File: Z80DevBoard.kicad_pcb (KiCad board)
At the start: 2 copper layers, 143 parts, among them SW1 WAIT, SW2 RESET, SW3 Z80BOOT, SW4 RPBOOT

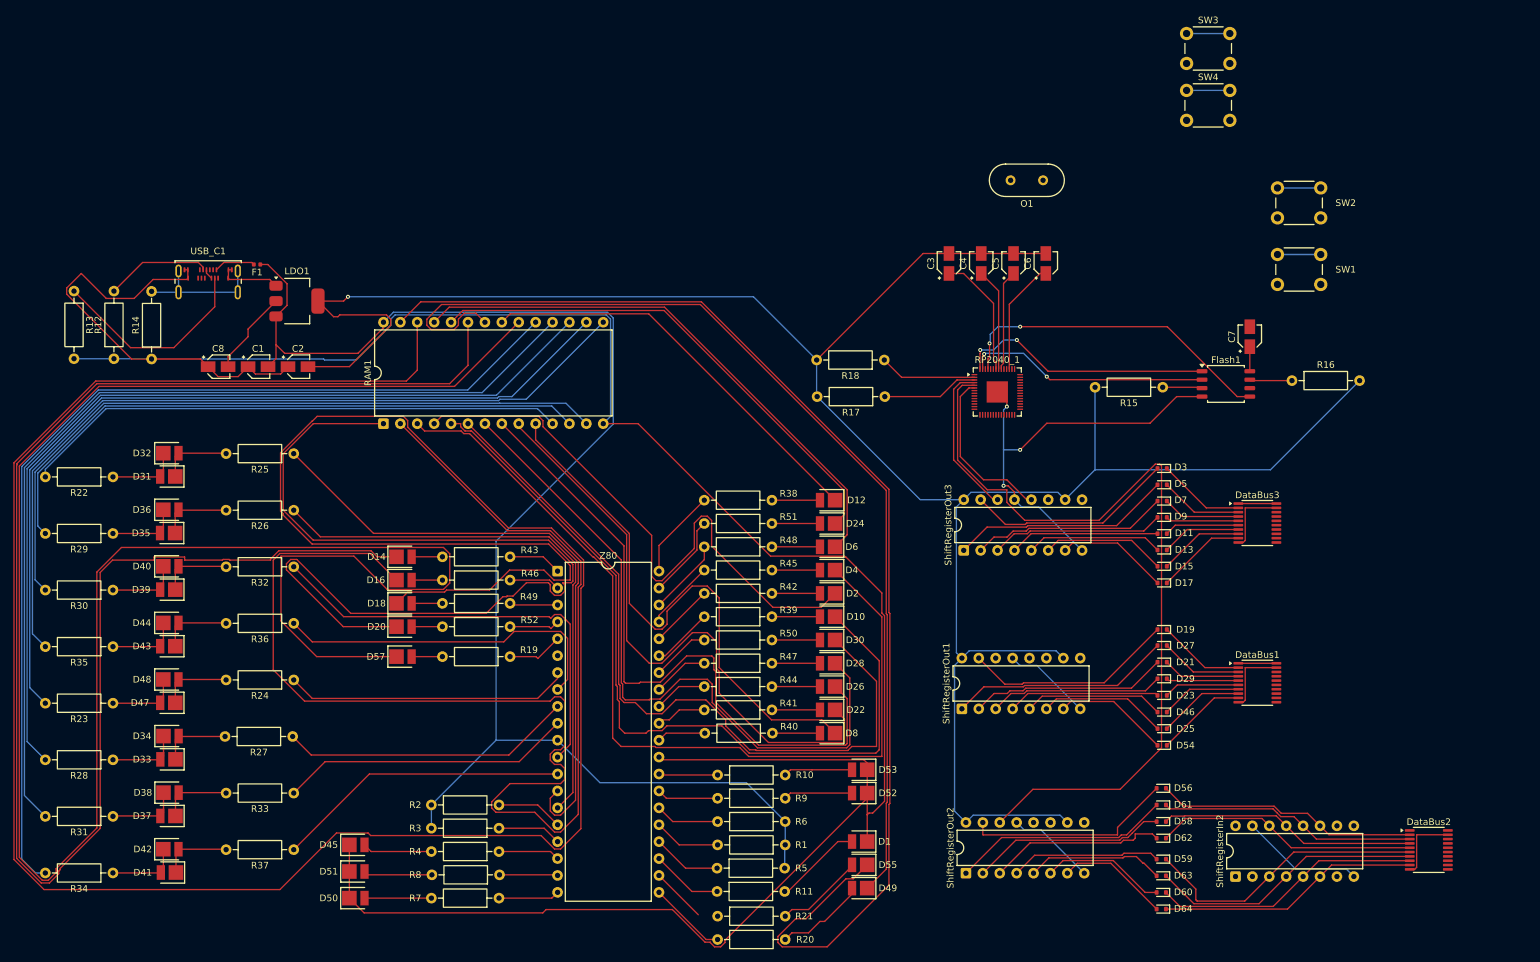
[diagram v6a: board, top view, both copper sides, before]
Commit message: Connected some pins of the RP2040. Connected the data bus to the RAM.
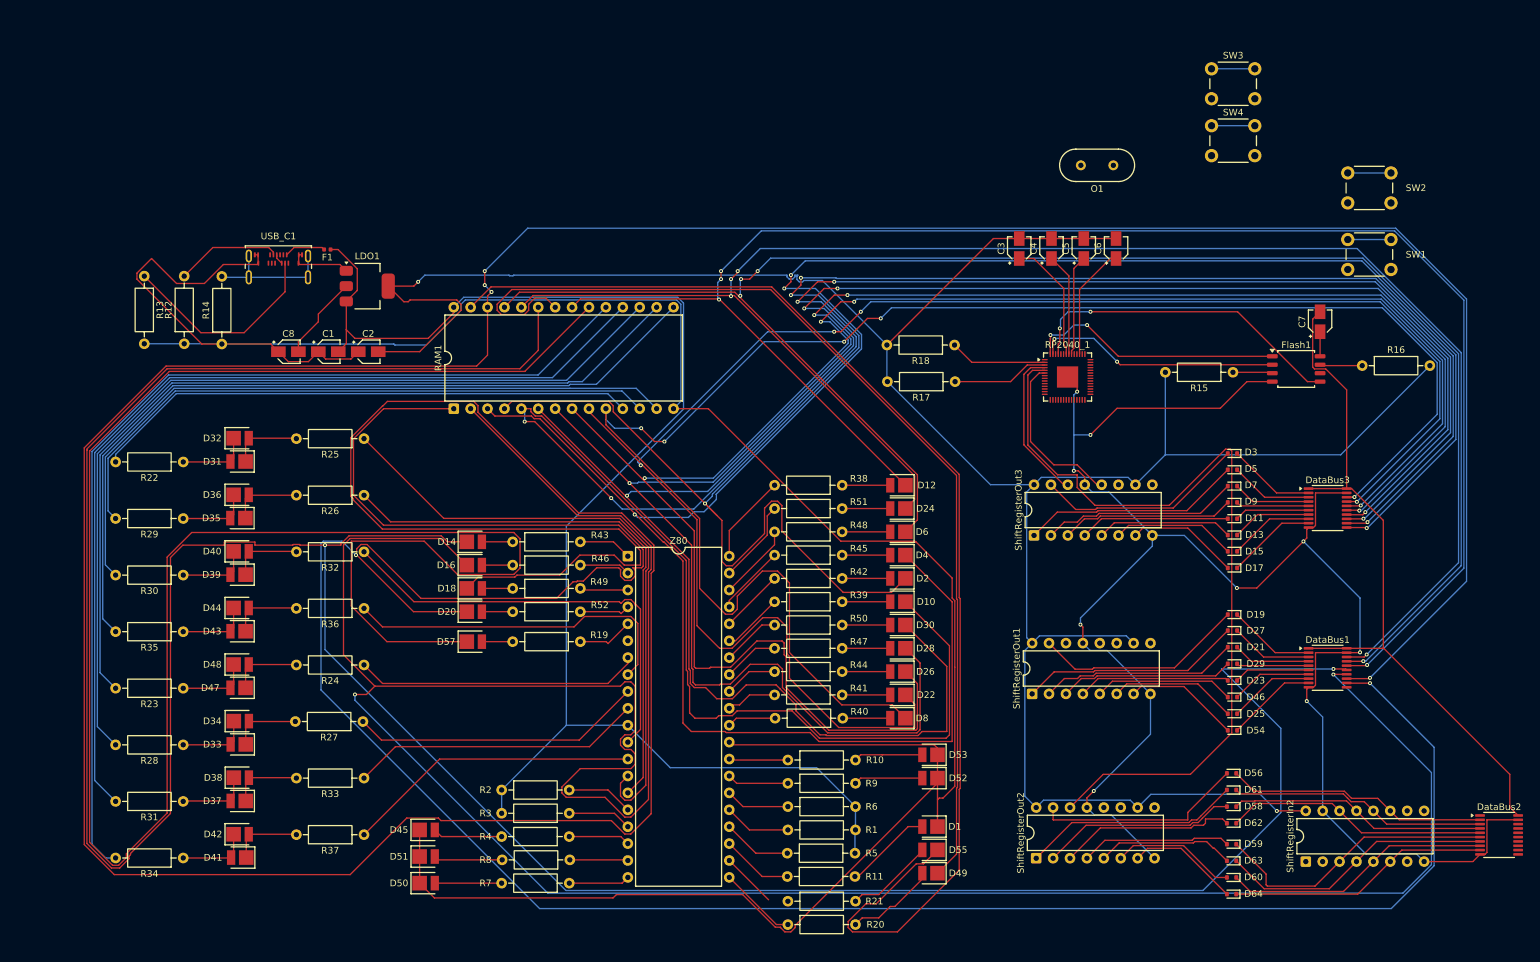
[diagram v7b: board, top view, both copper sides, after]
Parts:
- moved D56 10.8 mm to (212.8, 130.6)
- moved D58 10.8 mm to (212.8, 135.6)
- moved D61 10.8 mm to (212.8, 133.1)
- moved D62 10.8 mm to (212.8, 138.1)
- moved ShiftRegisterIn2 10.8 mm to (223.9, 143.9)
- moved ShiftRegisterOut2 10.8 mm to (183.4, 143.4)
- moved D10 10.8 mm to (162.9, 104.8)
- moved D12 10.8 mm to (162.9, 87.3)
- moved D2 10.8 mm to (162.9, 101.3)
- moved D22 10.8 mm to (162.9, 118.8)
- moved D24 10.8 mm to (162.9, 90.8)
- moved D26 10.8 mm to (162.9, 115.3)
- moved D28 10.8 mm to (162.9, 111.8)
- moved D30 10.8 mm to (162.9, 108.3)
- moved D4 10.8 mm to (162.9, 97.8)
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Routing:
- net RAM-A14: track 147.9 -> 394.6 mm, vias 0 -> 2
- net RAM-A13: track 410.6 -> 637.8 mm, vias 0 -> 4
- net RAM-A11: track 243.3 -> 466.6 mm, vias 0 -> 2
- net RAM-A12: track 200.8 -> 417.4 mm, vias 0 -> 2
- net RAM-A5: track 122.1 -> 338.4 mm, vias 0 -> 5
- net RAM-A7: track 135.7 -> 341.4 mm, vias 0 -> 4
- net RAM-A6: track 90.1 -> 279.8 mm, vias 0 -> 4
- net RAM-A4: track 113.6 -> 301.1 mm, vias 0 -> 4
- net RAM-A10: track 62.2 -> 249.1 mm, vias 0 -> 4
- net RAM-A3: track 104.5 -> 284.4 mm, vias 0 -> 4
- net RAM-A9: track 76.5 -> 252.5 mm, vias 0 -> 4
- net RAM-A2: track 100.4 -> 272.7 mm, vias 0 -> 4
- net RAM-A8: track 83.7 -> 255.5 mm, vias 0 -> 4
- net RAM-A0: track 84.5 -> 250.6 mm, vias 0 -> 5
- net RAM-A1: track 92.0 -> 254.9 mm, vias 0 -> 4
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
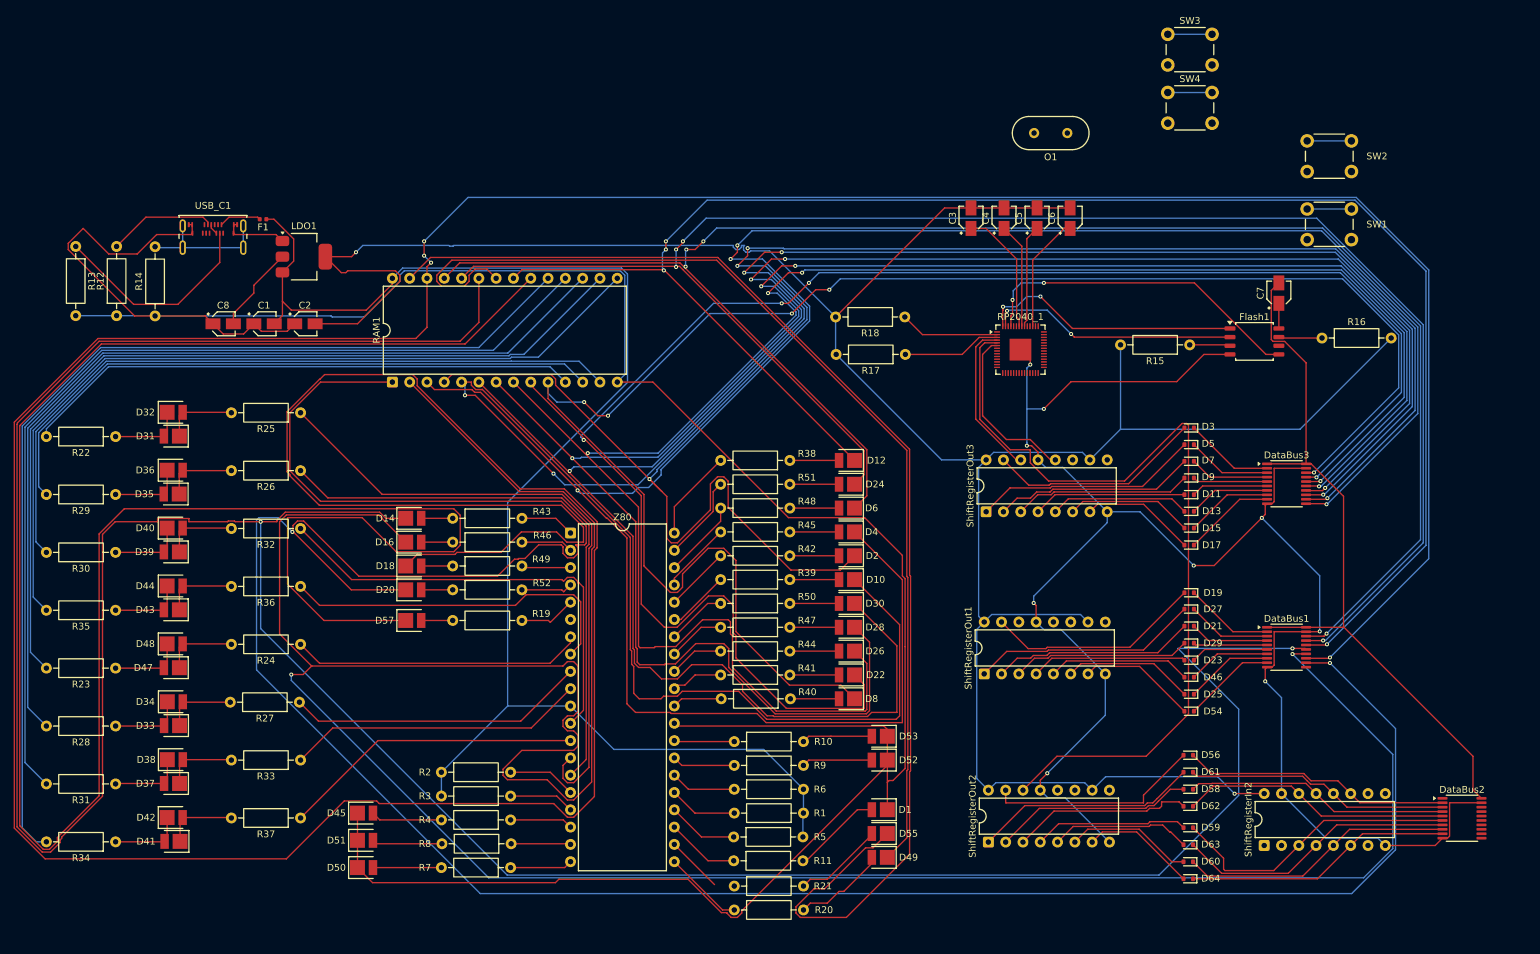
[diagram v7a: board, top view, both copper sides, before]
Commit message: Defined the boards. Positioned the last components. Do some connections. Semplified some old connections.
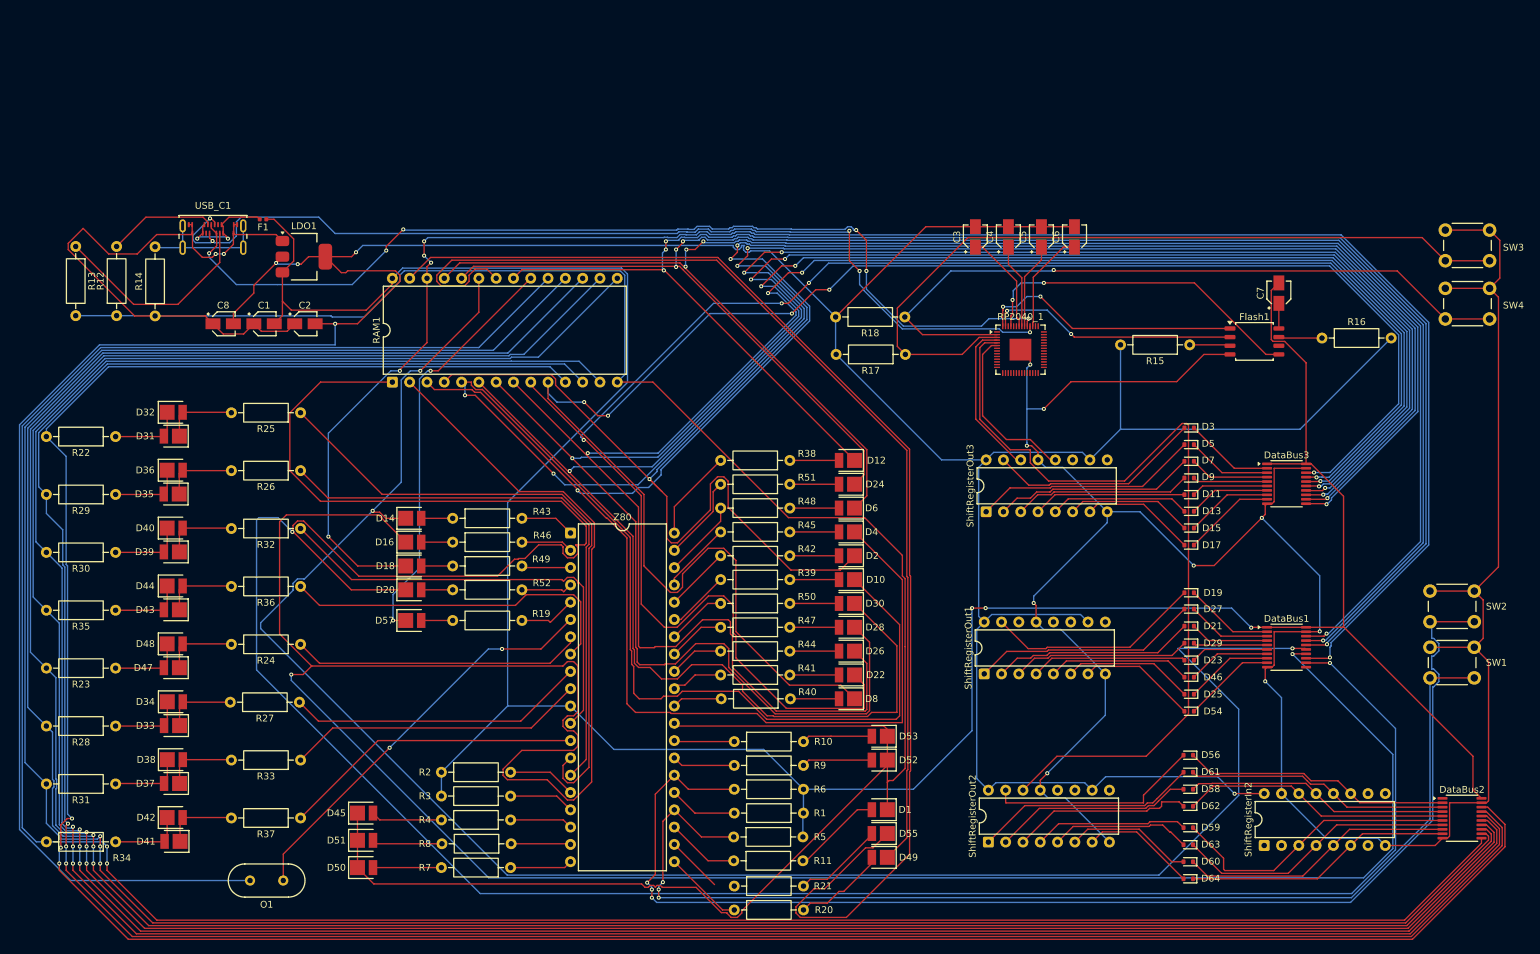
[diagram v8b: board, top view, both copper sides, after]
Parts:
- moved O1 159.0 mm to (79.9, 149.0)
- moved SW2 68.5 mm to (248.2, 106.5)
- moved SW1 66.8 mm to (248.2, 114.8)
- moved SW3 49.9 mm to (250.5, 53.5)
- moved SW4 49.9 mm to (250.5, 62.0)
- moved C6 2.82 mm to (196.1, 54.5)
- moved C3 2.82 mm to (181.5, 54.5)
- moved C4 2.82 mm to (186.3, 54.5)
- moved C5 2.82 mm to (191.2, 54.5)
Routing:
- net RAM-A13: track 637.8 -> 276.7 mm, vias 4 -> 6
- net RAM-Q0: track 82.0 -> 378.3 mm, vias 0 -> 3
- net RAM-Q1: track 94.7 -> 378.4 mm, vias 0 -> 3
- net RAM-Q2: track 106.7 -> 380.3 mm, vias 0 -> 3
- net RAM-Q3: track 122.2 -> 385.8 mm, vias 0 -> 3
- net RAM-Q4: track 128.8 -> 382.4 mm, vias 0 -> 3
- net RAM-CS: track 314.4 -> 61.4 mm, vias 0 -> 2
- net RAM-Q5: track 135.5 -> 379.0 mm, vias 0 -> 3
- net RAM-Q6: track 142.1 -> 376.0 mm, vias 0 -> 3
- net RAM-Q7: track 149.6 -> 372.5 mm, vias 0 -> 2
- net RAM-A11: track 466.6 -> 279.2 mm, vias 2 -> 3
- net Z80-RESET: track 9.66 -> 187.5 mm, vias 0 -> 3
- net Z80-WAIT: track 10.4 -> 169.5 mm, vias 0 -> 3
- net Vdd_3v3: track 387.7 -> 545.6 mm, vias 2 -> 5
- net USB-RP2040-DM: track 0.00 -> 145.7 mm, vias 0 -> 5
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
